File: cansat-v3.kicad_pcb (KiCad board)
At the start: 2 copper layers, 120 x 114.9 mm, 86 parts, among them J1 Conn_01x04_Socket, J2 USB_C_Receptacle_USB2.0_16P, J3 Micro_SD_Card, J4 Conn_01x02_Socket, J5 Conn_01x05_Socket, SW1 SW_Push, SW2 PWR, SW3 SW_Push, U1 ESP32-S3-WROOM-2, U10 MCP73871, U12 SCD40-D-R2, U13 BNO055, U14 AS7331-AQFM, U15 Digital PS, U2 BME680, U3 TSL25911FN, U5 Analog PS, U6 INA219BxDCN, U8 SRV05-4

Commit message: Layout
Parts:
- C19, C20, C21, R29, R30, R31: moved to B.Cu
- moved R34 245.6 mm to (170.0, 118.6)
- moved R35 245.0 mm to (170.0, 117.1)
- moved C23 242.5 mm to (167.6, 114.3)
- moved R33 240.3 mm to (164.8, 116.3), turned to -90 degrees
- moved R7 230.7 mm to (172.6, 86.1)
- moved R4 230.3 mm to (172.6, 87.6), turned to 180 degrees
- moved C6 223.2 mm to (175.6, 88.5)
- moved C7 217.2 mm to (176.3, 90.7), turned to 90 degrees
- moved C22 211.8 mm to (167.1, 119.9)
- moved C20 200.5 mm to (148.5, 103.2)
- moved R29 197.2 mm to (145.0, 100.7), turned to -90 degrees
- moved C19 191.3 mm to (146.5, 100.7), turned to -90 degrees
- moved C21 189.0 mm to (148.3, 97.0), turned to -90 degrees
- moved R30 187.7 mm to (154.3, 99.7)
- moved R31 187.6 mm to (154.3, 98.2)
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
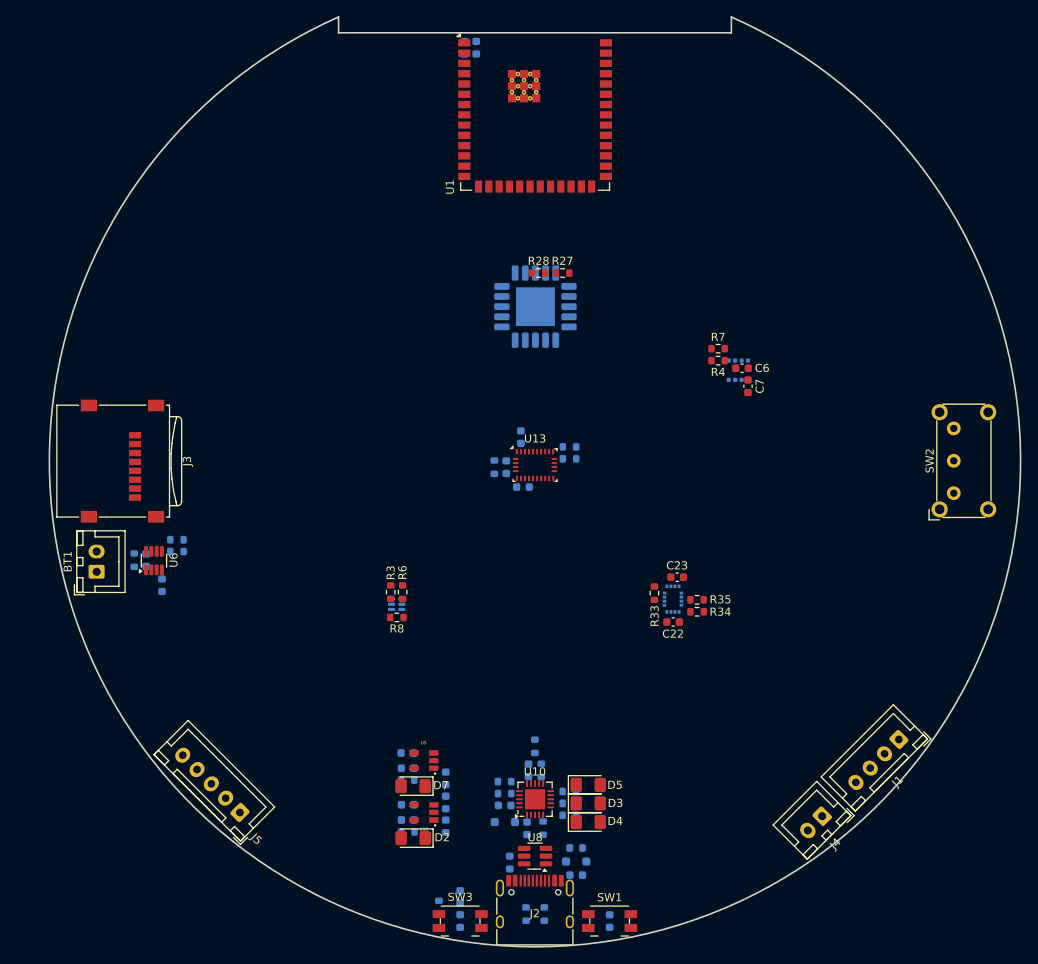
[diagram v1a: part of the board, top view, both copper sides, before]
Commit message: Component placement finished, started routing
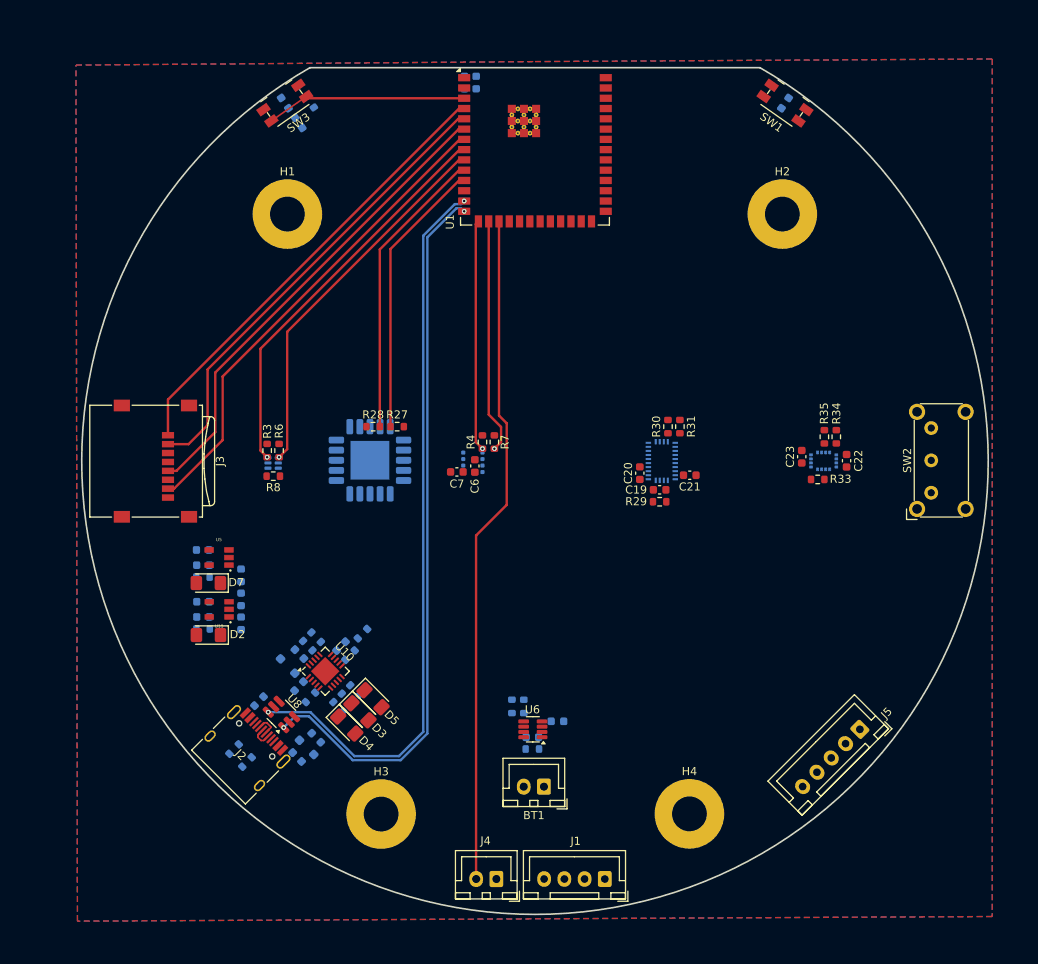
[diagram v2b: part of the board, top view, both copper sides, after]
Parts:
- added H1: MountingHole_Pad, MountingHole:MountingHole_4.3mm_M4_Pad, F.Cu at (119.4, 69.5)
- added H2: MountingHole_Pad, MountingHole:MountingHole_4.3mm_M4_Pad, F.Cu at (180.6, 69.5)
- added H3: MountingHole_Pad, MountingHole:MountingHole_4.3mm_M4_Pad, F.Cu at (131.0, 143.6)
- added H4: MountingHole_Pad, MountingHole:MountingHole_4.3mm_M4_Pad, F.Cu at (169.1, 143.6)
- C19, C20, C21, R29, R30, R31: moved to F.Cu
- U13: moved to B.Cu
- moved C5 103.4 mm to (180.9, 55.8), turned to 55 degrees
- moved SW1 103.4 mm to (180.9, 55.8), turned to -35 degrees
- moved C2 103.4 mm to (119.1, 55.8), turned to 125 degrees
- moved SW3 103.4 mm to (119.1, 55.8), turned to 35 degrees
- moved R1 100.8 mm to (122.2, 55.6), turned to 125 degrees
- moved C1 97.7 mm to (120.8, 58.2), turned to 125 degrees
- moved J5 77.3 mm to (190.1, 133.1), turned to -135 degrees
- moved BT1 61.3 mm to (151.1, 140.2), turned to 180 degrees
- moved R9 54.5 mm to (149.7, 135.6), turned to 180 degrees
- moved C10 52.5 mm to (149.7, 134.1), turned to 180 degrees
- moved C12 51.7 mm to (152.8, 132.1), turned to 180 degrees
- moved U6 51.3 mm to (149.7, 133.1), turned to 180 degrees
- moved R11 46.9 mm to (148.6, 130.3), turned to -90 degrees
- moved R10 46.2 mm to (147.1, 130.3), turned to -90 degrees
- moved R24 41.4 mm to (112.8, 135.6), turned to -135 degrees
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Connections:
- U1 pad 10: unconnected-(U1-IO17-Pad10) -> SCD40_SCL
- U1 pad 11: unconnected-(U1-IO18-Pad11) -> SCD40_SDA
- U1 pad 13: unconnected-(U1-USB_D-/IO19-Pad13) -> USB_D-
- U1 pad 14: unconnected-(U1-USB_D+/IO20-Pad14) -> USB_D+
- U1 pad 15: unconnected-(U1-IO3-Pad15) -> BME680_SCL
- U1 pad 16: unconnected-(U1-IO46-Pad16) -> BME680_SDA
- U1 pad 17: unconnected-(U1-IO9-Pad17) -> COMPASS_SCL
- U1 pad 18: unconnected-(U1-IO10-Pad18) -> COMPASS_SDA
- U1 pad 19: unconnected-(U1-IO11-Pad19) -> INA219_SDA
- U1 pad 20: unconnected-(U1-IO12-Pad20) -> INA219_SCL
- U1 pad 21: unconnected-(U1-IO13-Pad21) -> GPS_RX
- U1 pad 22: unconnected-(U1-IO14-Pad22) -> GPS_TX
- U1 pad 23: unconnected-(U1-IO21-Pad23) -> BNO055_RST
- U1 pad 26: unconnected-(U1-IO45-Pad26) -> BNO055_SDA
- U1 pad 31: unconnected-(U1-IO38-Pad31) -> BNO055_SCL
- U1 pad 32: unconnected-(U1-MTCK/IO39-Pad32) -> LoRa_RST
- U1 pad 33: unconnected-(U1-MTDO/IO40-Pad33) -> AS7331_SCL
- U1 pad 34: unconnected-(U1-MTDI/IO41-Pad34) -> AS7331_SDA
- U1 pad 36: unconnected-(U1-RXD0/IO44-Pad36) -> LoRa_RX
- U1 pad 37: unconnected-(U1-TXD0/IO43-Pad37) -> LoRa_TX
- U1 pad 4: unconnected-(U1-IO4-Pad4) -> SD_CS
- U1 pad 5: unconnected-(U1-IO5-Pad5) -> SD_MOSI
- U1 pad 6: unconnected-(U1-IO6-Pad6) -> SD_CLK
- U1 pad 7: unconnected-(U1-IO7-Pad7) -> SD_MISO
- U1 pad 8: unconnected-(U1-IO15-Pad8) -> TSL2591_SDA
- U1 pad 9: unconnected-(U1-IO16-Pad9) -> TSL2591_SCL
- U8 pad 1: USB_D- -> USB_D+
- U8 pad 6: USB_D+ -> USB_D-
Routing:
- net USB_D-: track 0.00 -> 93.7 mm, vias 0 -> 2
- net USB_D+: track 0.00 -> 92.3 mm, vias 0 -> 2
- net COMPASS_SCL: track 0.00 -> 83.2 mm
- net SD_MISO: track 0.00 -> 59.1 mm
- net SD_CLK: track 0.00 -> 58.4 mm
- net SD_MOSI: track 0.00 -> 57.3 mm
- net SD_CS: track 0.00 -> 55.9 mm
- net TSL2591_SDA: track 0.00 -> 49.1 mm, vias 0 -> 1
- net TSL2591_SCL: track 0.00 -> 46.6 mm, vias 0 -> 1
- net SCD40_SCL: track 0.00 -> 36.4 mm
- net SCD40_SDA: track 0.00 -> 34.6 mm
- net BME680_SDA: track 0.00 -> 29.1 mm, vias 0 -> 1
- net BME680_SCL: track 0.00 -> 28.6 mm, vias 0 -> 1
- net /RST: track 0.00 -> 24.9 mm
- added copper zone on B.Cu, net GND
- added copper zone on F.Cu, net GND
- added copper zone on In1.Cu, net GND
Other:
- board size 120 x 114.9 mm -> 112 x 104.6 mm
- copper layers 2 -> 4
